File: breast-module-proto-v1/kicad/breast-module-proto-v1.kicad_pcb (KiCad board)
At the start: 2 copper layers, 110 x 90 mm, 96 parts, among them J1 USB_C_Receptacle_USB2.0, J2 Conn_01x06_Male, J3 Conn_01x06_Male, J4 SWD, Q1 SS8050-G, Q2 SS8050-G, U1 AMS1117-3.3, U10 74HC00, U11 IRM-H6XXT, U12 IRM-H6XXT, U13 STM32G030Fx, U2 TP4056, U3 TPS61230ARNSR, U4 DW01, U5 FS8205A, U6 74HC00, U7 ESP32-WROOM-32, U8 USBLC6-2SC6, U9 CP2102N-Axx-xQFN28

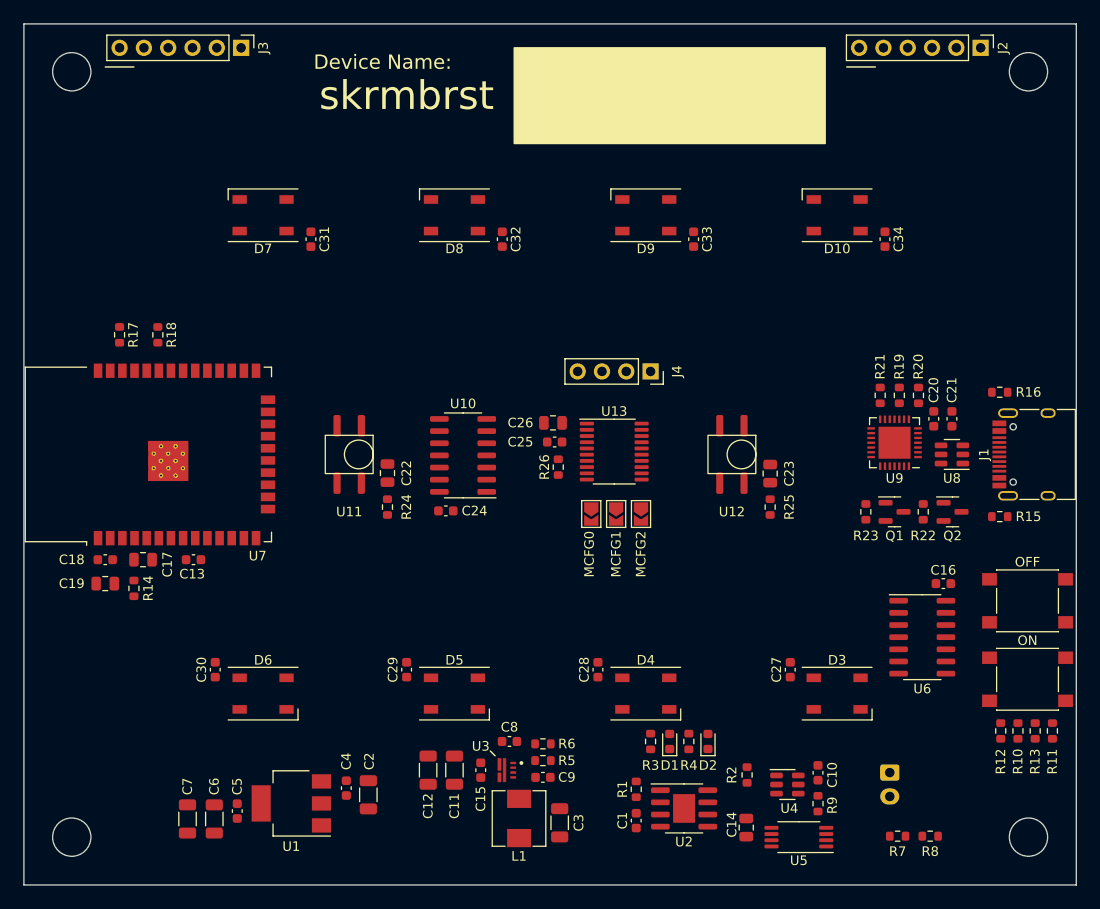
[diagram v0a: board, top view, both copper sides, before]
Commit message: Rendering almost done (power rails missing)
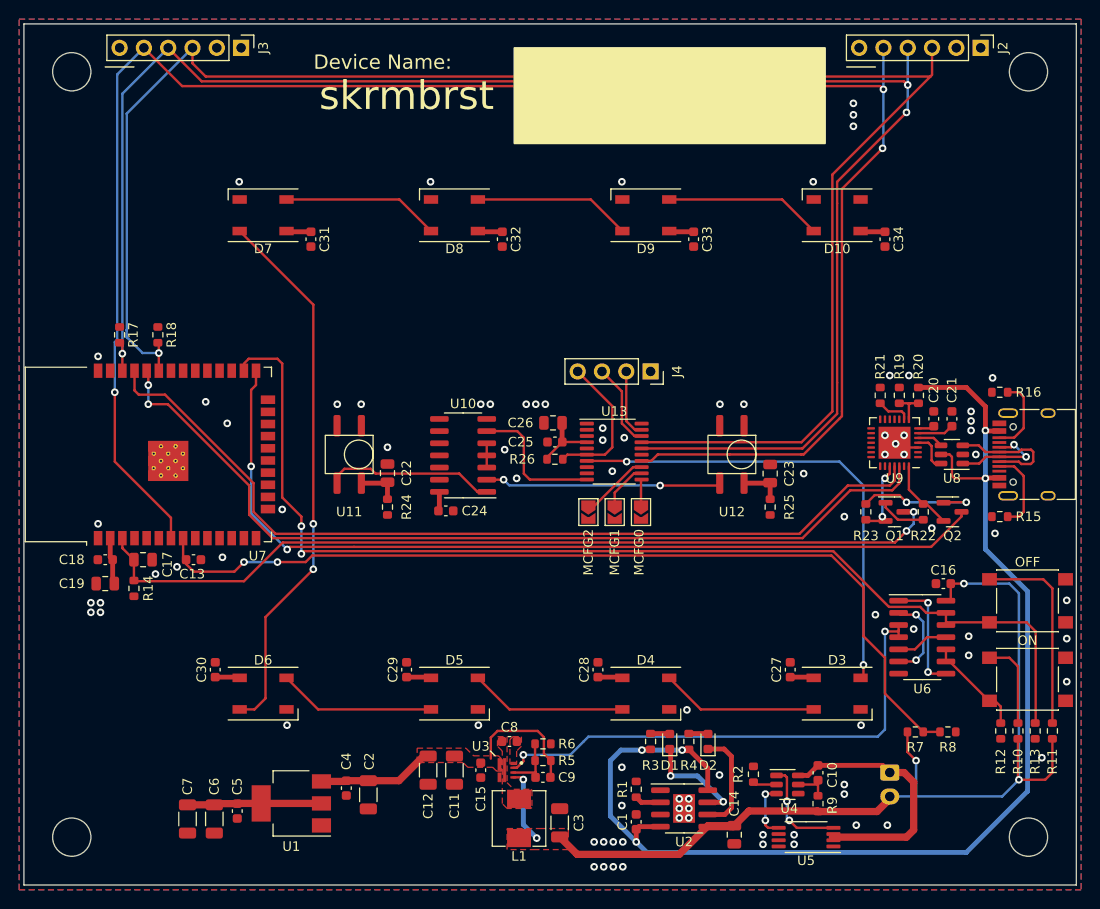
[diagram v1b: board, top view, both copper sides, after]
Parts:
- moved R7 11.1 mm to (183.7, 125.5)
- moved R8 11.1 mm to (187.1, 125.5)
- moved MCFG2 5.50 mm to (149.5, 102.5)
- moved MCFG0 5.20 mm to (155.0, 102.5)
- moved C14 1.46 mm to (164.8, 136.2)
- moved R26 0.90 mm to (146.0, 97.0), turned to 0 degrees
- moved U5 0.75 mm to (172.2, 136.5)
- moved R2 0.67 mm to (166.8, 129.9)
- moved MCFG1 0.25 mm to (152.2, 102.5)
- moved C1 0.13 mm to (154.5, 134.9)
- turned R16 to 180 degrees
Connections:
- U2 pad 9: unconnected-(U2-Pad9) -> GND
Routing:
- net HP_IRQ: track 0.00 -> 197.2 mm, vias 0 -> 3
- net I2C_SDA: track 0.00 -> 183.0 mm, vias 0 -> 1
- net I2C_SCL: track 0.00 -> 179.1 mm, vias 0 -> 3
- net VBUS: track 0.00 -> 131.9 mm, vias 0 -> 5
- net PWR_OFF: track 0.00 -> 116.0 mm, vias 0 -> 2
- net BAT_P: track 0.00 -> 110.9 mm, vias 0 -> 5
- net VBAT_MEASURE: track 0.00 -> 95.5 mm, vias 0 -> 2
- net ESP_RXD: track 0.00 -> 93.8 mm, vias 0 -> 2
- net ESP_TXD: track 0.00 -> 93.3 mm
- net ESP_IO0: track 0.00 -> 92.9 mm, vias 0 -> 2
- net ESP_EN: track 0.00 -> 91.3 mm, vias 0 -> 2
- net Net-(D6-Pad2): track 0.00 -> 57.3 mm, vias 0 -> 2
- net PWR_EN: track 0.00 -> 53.9 mm, vias 0 -> 2
- net LED_DIN: track 0.00 -> 50.2 mm, vias 0 -> 2
- net +5V: track 0.00 -> 45.6 mm
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- added copper zone on F.Cu, net +5V
- added copper zone on F.Cu, net BAT_P
- added copper zone on B.Cu, net GND
- added copper zone on F.Cu, net GND
- added copper zone on F.Cu, net Net-(C8-Pad1)
- added copper zone on F.Cu, net Net-(C8-Pad2)

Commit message: Routing finished
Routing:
- net +3V3: track 33.7 -> 356.5 mm, vias 0 -> 10
- net +5V: track 45.6 -> 294.5 mm, vias 0 -> 11
- net GND: vias 88 -> 217
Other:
- board text added: "Skirmish Breast Module (Proto V1) Design / (C) 2023 Ole Lange"
